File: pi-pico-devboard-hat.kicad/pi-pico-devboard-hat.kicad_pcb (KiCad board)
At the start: 2 copper layers, 65 x 56 mm, 16 parts, among them J1 Conn_01x24_Male, J2 I2C, J3 SDA_UP, J4 SCL_UP, J5 Conn_SPI, J6 Conn_Ext, P1 Conn_02x20_Odd_Even, SW1 SW_Reset, U1 Pico

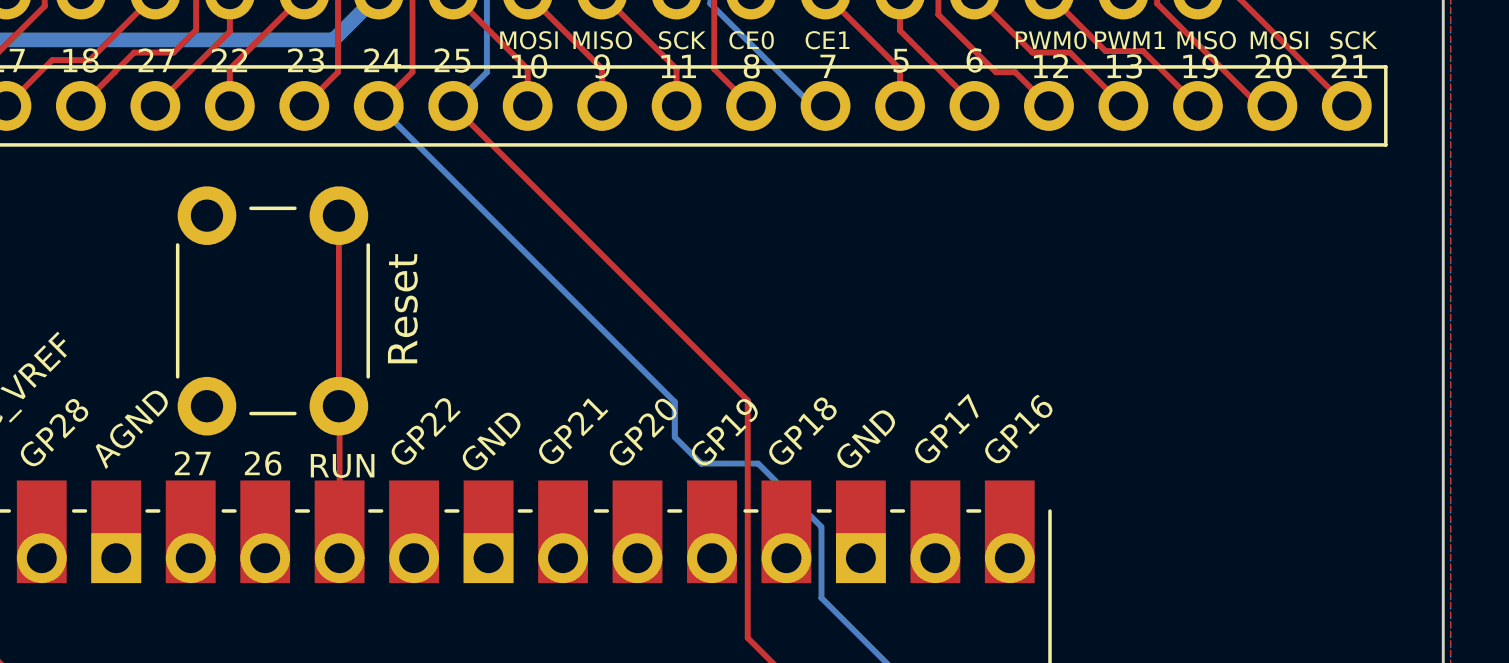
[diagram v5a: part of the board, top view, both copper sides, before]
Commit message: Rev 6: added buttons
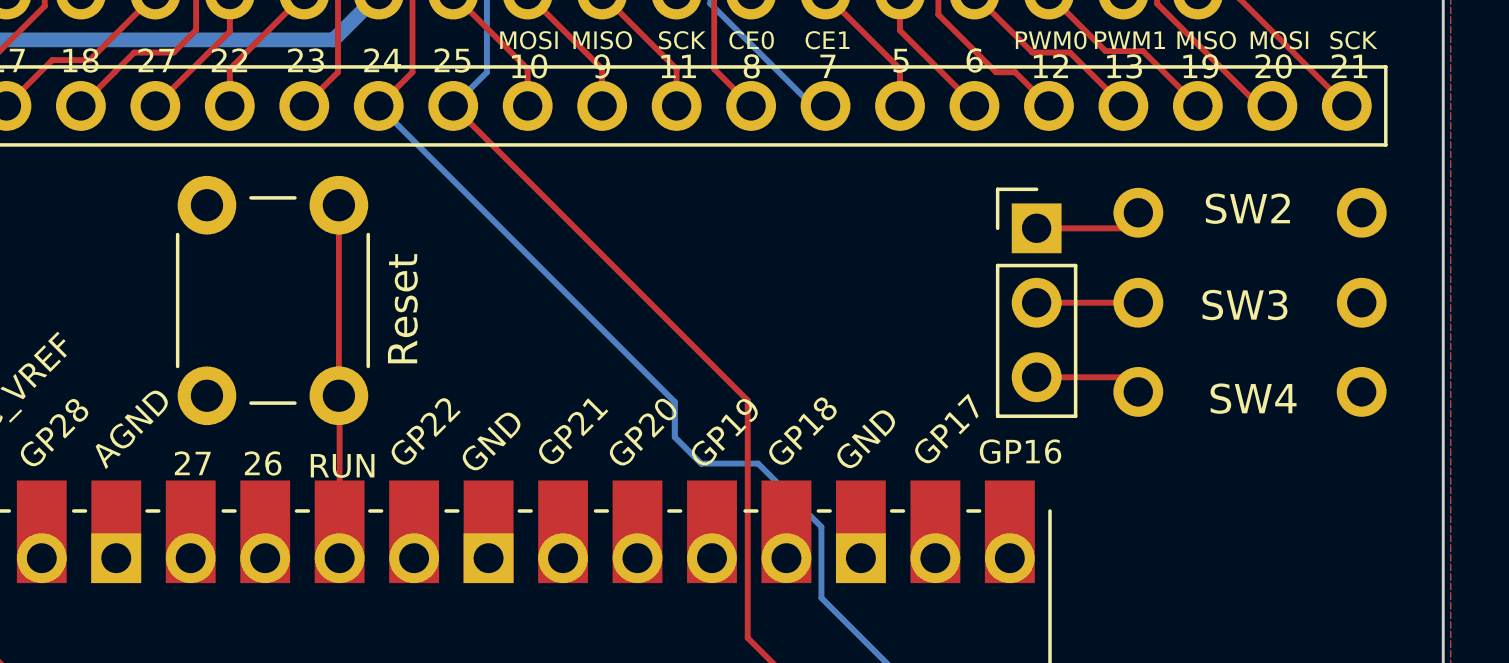
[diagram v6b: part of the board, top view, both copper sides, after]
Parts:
- added J7: Conn_BTN, Connector_PinHeader_2.54mm:PinHeader_1x03_P2.54mm_Vertical, F.Cu at (251.1, 106.7)
- added SW2: BTN1, user:SW_PUSH_SLIM_1x4, F.Cu at (254.6, 106.2)
- added SW3: BTN2, user:SW_PUSH_SLIM_1x4, F.Cu at (254.6, 109.3)
- added SW4: BTN3, user:SW_PUSH_SLIM_1x4, F.Cu at (254.6, 112.3)
- moved SW1 0.36 mm to (227.3, 106.0)
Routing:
- net Net-(J7-Pad1): track 0.00 -> 3.69 mm
- net Net-(J7-Pad3): track 0.00 -> 3.67 mm
- net Net-(J7-Pad2): track 0.00 -> 3.47 mm
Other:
- board text added: "Rev: 6"
- board text removed: "Rev: 5"

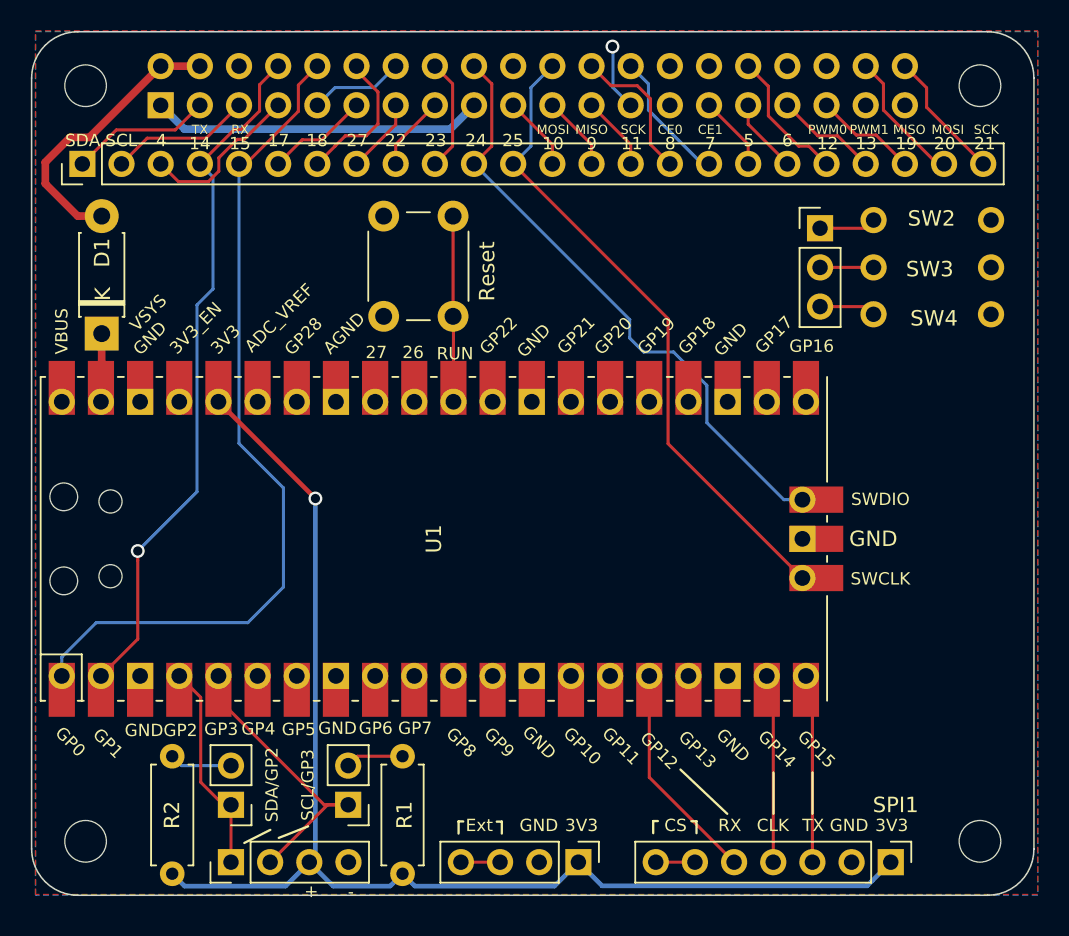
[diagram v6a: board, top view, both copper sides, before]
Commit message: Rev 7: added LEDs
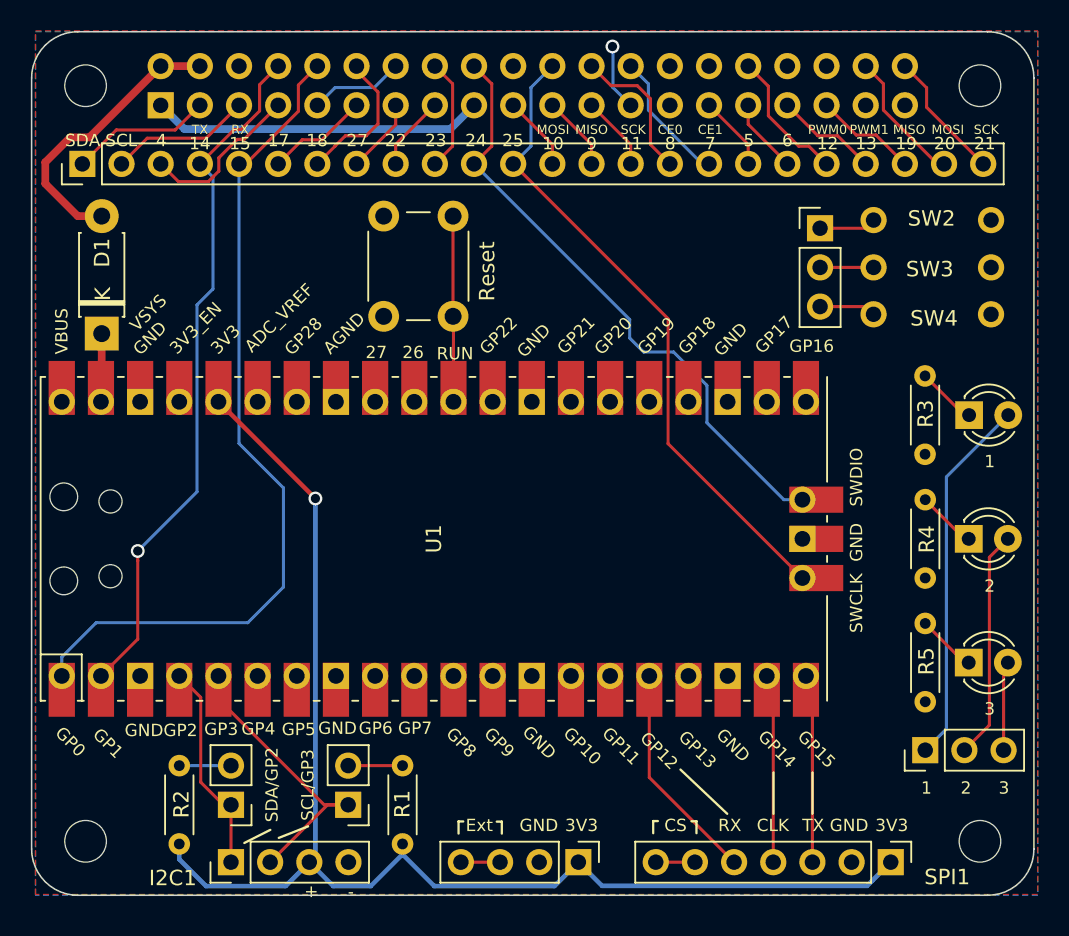
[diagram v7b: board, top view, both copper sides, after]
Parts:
- added D2: LED, LED_THT:LED_D3.0mm, F.Cu at (260.8, 118.9)
- added D3: LED, LED_THT:LED_D3.0mm, F.Cu at (260.8, 126.9)
- added D4: LED, LED_THT:LED_D3.0mm, F.Cu at (260.8, 134.9)
- added J8: Conn_LED, Connector_PinHeader_2.54mm:PinHeader_1x03_P2.54mm_Vertical, F.Cu at (258.0, 140.6)
- added R3: 680Ω, Resistor_THT:R_Axial_DIN0204_L3.6mm_D1.6mm_P5.08mm_Horizontal, F.Cu at (257.9, 121.4)
- added R4: 680Ω, Resistor_THT:R_Axial_DIN0204_L3.6mm_D1.6mm_P5.08mm_Horizontal, F.Cu at (258.0, 129.4)
- added R5: 680Ω, Resistor_THT:R_Axial_DIN0204_L3.6mm_D1.6mm_P5.08mm_Horizontal, F.Cu at (258.0, 137.5)
- R1, R2: footprint Resistor_THT:R_Axial_DIN0207_L6.3mm_D2.5mm_P7.62mm_Horizontal -> Resistor_THT:R_Axial_DIN0204_L3.6mm_D1.6mm_P5.08mm_Horizontal
- moved R2 1.98 mm to (209.6, 146.7)
- moved R1 1.93 mm to (224.1, 146.7)
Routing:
- net Net-(D2-Pad2): track 0.00 -> 24.0 mm
- net Net-(D3-Pad2): track 0.00 -> 14.9 mm
- net Net-(D4-Pad2): track 0.00 -> 5.79 mm
- net Net-(D2-Pad1): track 0.00 -> 3.91 mm
- net Net-(D4-Pad1): track 0.00 -> 3.87 mm
- net Net-(D3-Pad1): track 0.00 -> 3.87 mm
- net /3V3: track 84.7 -> 86.1 mm
- net Net-(J4-Pad2): track 4.06 -> 3.35 mm
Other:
- board text added: "1"
- board text added: "2"
- board text added: "3"
- board text added: "I2C1"
- board text added: "Rev: 7"
- board text removed: "Rev: 6"

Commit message: Rev 8: added power-connector / fine-tuning
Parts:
- added J9: Conn_02x03_Odd_Even, Connector_PinHeader_2.54mm:PinHeader_2x03_P2.54mm_Vertical, F.Cu at (212.1, 108.8)
- J5: footprint Connector_PinHeader_2.54mm:PinHeader_1x07_P2.54mm_Vertical -> Connector_PinHeader_2.54mm:PinHeader_1x06_P2.54mm_Vertical
- J6: footprint Connector_PinHeader_2.54mm:PinHeader_1x04_P2.54mm_Vertical -> Connector_PinHeader_2.54mm:PinHeader_1x03_P2.54mm_Vertical
- moved J6 3.02 mm to (232.4, 147.9)
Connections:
- J5 pad 6: Net-(J5-Pad6) -> /SPI_CS_GP13
- J6 pad 3: Net-(J6-Pad3) -> /GP8
- U1 pad 11: Net-(U1-Pad11) -> /GP8
- U1 pad 17: Net-(U1-Pad17) -> /SPI_CS_GP13
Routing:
- net /3V3: track 86.1 -> 100.3 mm
- net /SPI_CS_GP13: track 0.00 -> 12.3 mm
- net /GP8: track 0.00 -> 12.1 mm
- net Net-(J5-Pad6): track 2.54 -> 0.00 mm
- net Net-(J6-Pad3): track 2.54 -> 0.00 mm
- net /GPIO14(TXD0): track 45.3 -> 44.6 mm
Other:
- board text added: "Rev: 8"
- board text added: "UART0 -> Pi"
- board text removed: "Rev: 7"
